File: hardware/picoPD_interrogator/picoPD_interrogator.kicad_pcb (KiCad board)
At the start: 4 copper layers, 81.9 x 17.2 mm, 94 parts, among them J4 Extra Pins, J5 Conn_01x04, J6 SM03B-SRSS-TB, J7 SM04B-SRSS-TB, Q1 rohm-RE1C002UN, Q2 rohm-RE1C002UN, Q3 rohm-RE1C002UN, Q4 rohm-RE1C002UN, Q5 rohm-RE1C002UN, Q6 rohm-RE1C002UN, SW1 SW_Push, SW2 SW_Push, U1 RP2350_60QFN, U10 W25Q128JVS, U2 ST-LM393QT, U7 LV2862XDDC, Y1 Crystal_GND24

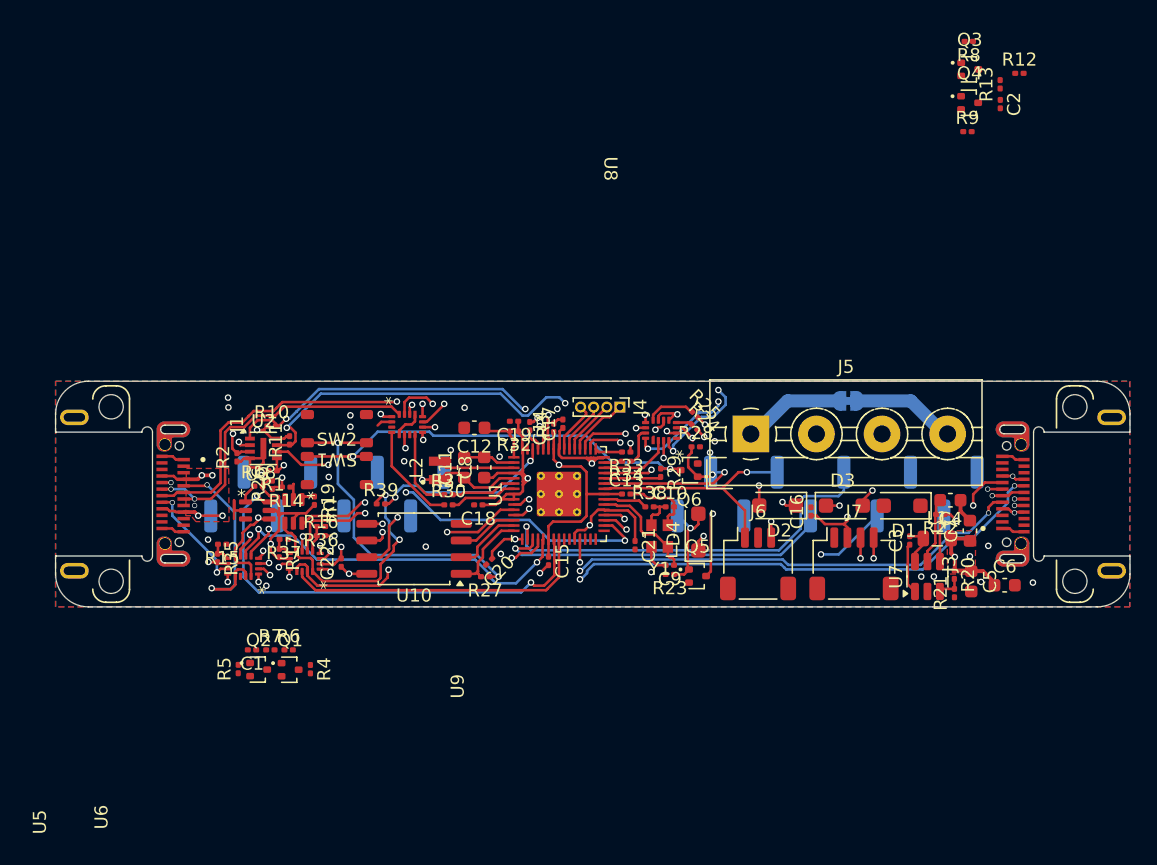
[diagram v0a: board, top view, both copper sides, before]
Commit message: Routed almost everything. Just need to finish VBUS tracks and check for any obvious issues.
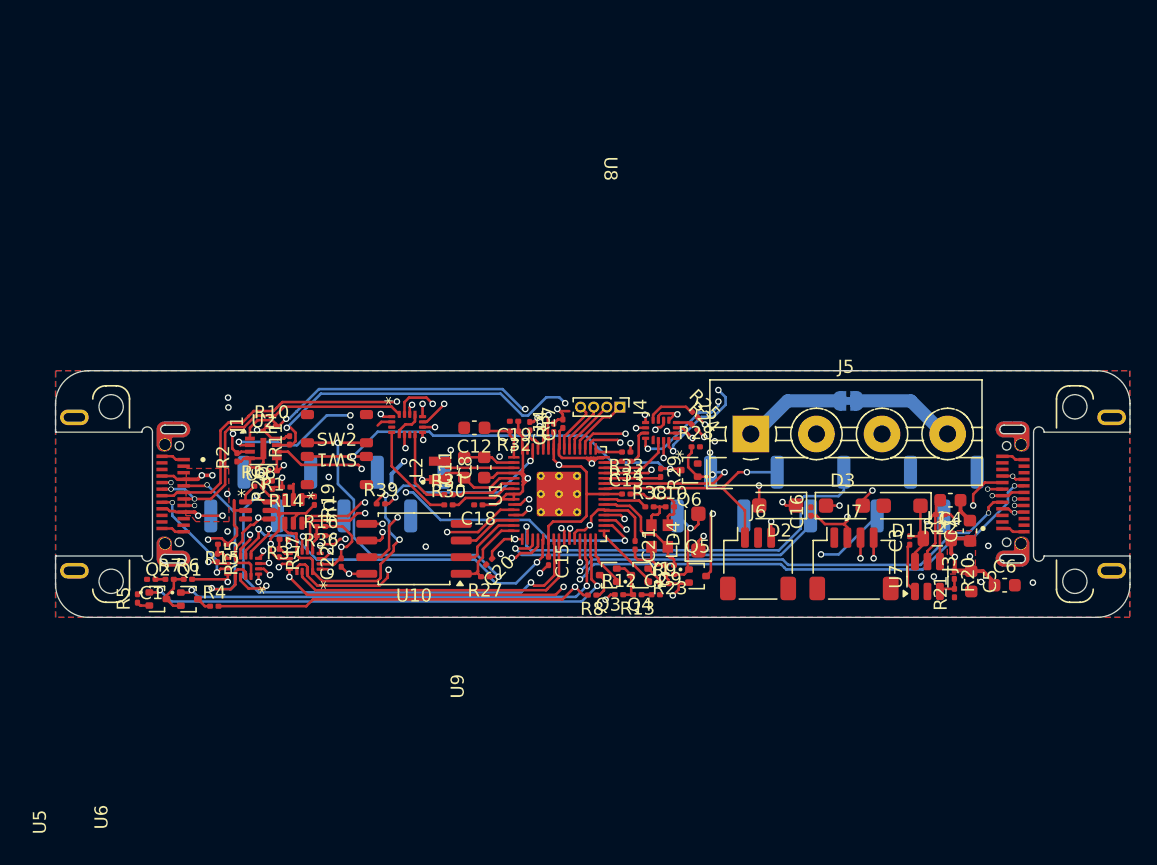
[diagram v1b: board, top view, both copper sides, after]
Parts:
- moved R8 51.0 mm to (158.4, 107.7)
- moved R12 50.1 mm to (160.4, 107.7)
- moved R13 47.7 mm to (161.8, 107.7), turned to 180 degrees
- moved Q3 47.4 mm to (159.6, 106.2), turned to 180 degrees
- moved C2 45.7 mm to (163.2, 107.7), turned to 0 degrees
- moved Q4 43.9 mm to (162.0, 106.2), turned to 180 degrees
- moved R9 41.5 mm to (163.9, 106.8)
- moved R5 9.38 mm to (123.7, 108.0)
- moved R6 9.38 mm to (127.6, 106.5)
- moved R7 9.38 mm to (126.2, 106.5)
- moved C1 9.38 mm to (124.8, 106.5)
- moved Q1 9.38 mm to (127.7, 108.0)
- moved Q2 9.38 mm to (125.3, 108.0)
- moved R4 8.76 mm to (129.6, 108.5), turned to 0 degrees
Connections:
- Q3 pad 2: /USB_PD/P0_TX -> /USB_PD/P1_TX
- Q4 pad 3: /USB_PD/P0_TX -> /USB_PD/P1_TX
- R12 pad 2: /USB_PD/P0_TX -> /USB_PD/P1_TX
- R13 pad 2: /USB_PD/P0_TX -> /USB_PD/P1_TX
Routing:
- net /P1_CC_RX: track 26.8 -> 66.5 mm, vias 2 -> 4
- net /P0_TX_L: track 0.00 -> 38.9 mm, vias 0 -> 2
- net /P0_CC_RX: track 24.3 -> 60.2 mm, vias 2 -> 4
- net /P0_TX_H: track 0.00 -> 35.2 mm, vias 0 -> 2
- net /P1_CC: track 35.4 -> 65.7 mm, vias 5 -> 9
- net /3V3: track 75.1 -> 104.1 mm, vias 16 -> 17
- net GND: track 38.1 -> 59.5 mm, vias 17 -> 18
- net /REG_VIN: track 7.53 -> 20.1 mm, vias 2 -> 3
- net /P0_CC: track 42.1 -> 54.5 mm, vias 6 -> 5
- net /RP2350A/1V1: track 24.6 -> 35.5 mm
- net /P1_TX_L: track 0.00 -> 5.27 mm
- net /P1_TX_H: track 0.00 -> 3.91 mm
- net /USB_PD/P0_TX: track 0.00 -> 3.80 mm
- net /USB_PD/P1_TX: track 0.00 -> 3.62 mm
- net /P0_ORIENT: track 22.7 -> 25.3 mm
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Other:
- board size 81.9 x 17.2 mm -> 81.9 x 18.8 mm

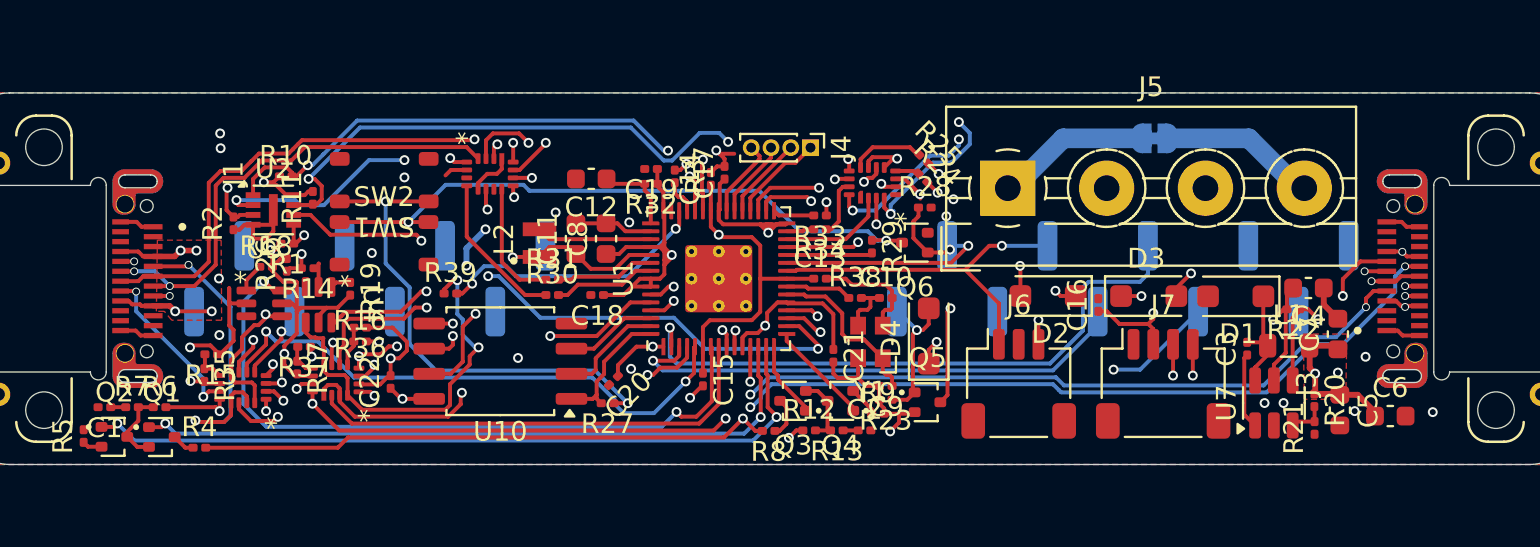
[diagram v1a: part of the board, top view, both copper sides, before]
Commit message: PCB: Resolve a bunch of clearance DRC errors.
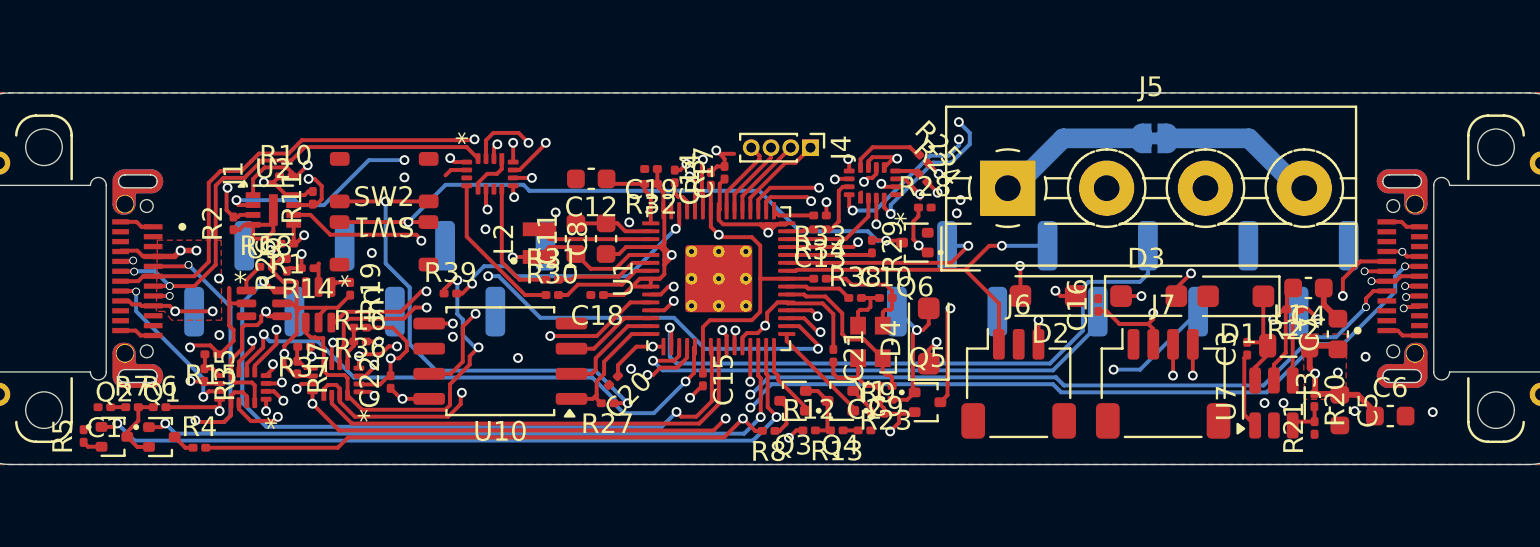
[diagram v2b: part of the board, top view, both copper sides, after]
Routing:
- net /P1_CC_RX: track 66.5 -> 42.8 mm, vias 4 -> 3
- net /P0_CC_RX: track 60.2 -> 40.4 mm, vias 4 -> 3
- net /P0_CC: track 54.5 -> 58.3 mm
- net /P0_VBUS: track 23.8 -> 26.3 mm
- net /P1_CC: track 65.7 -> 63.5 mm, vias 9 -> 8
- net /P0_VCONN: track 36.0 -> 37.2 mm
- net /P1_VBUS: track 20.6 -> 19.7 mm
- net /RP2_RESET: track 20.1 -> 20.9 mm
- net /USB_PD/P0_SBU2: vias 4 -> 3
- net /USB_PD/P0_SBU1: vias 3 -> 2

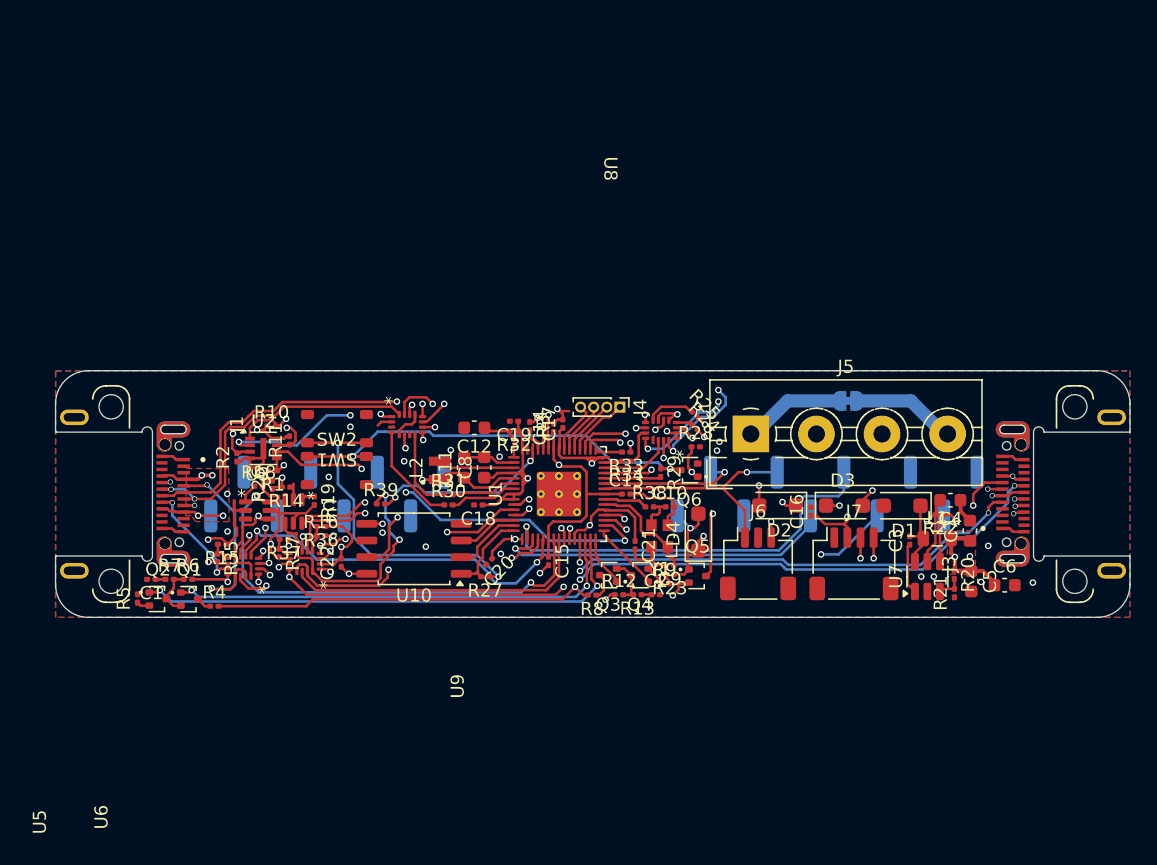
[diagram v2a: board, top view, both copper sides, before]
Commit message: Footprint/PCB: Modified JAE USB-C connector to have plated through-hole for the screw mount holes. Fixed missing SPI flash track.
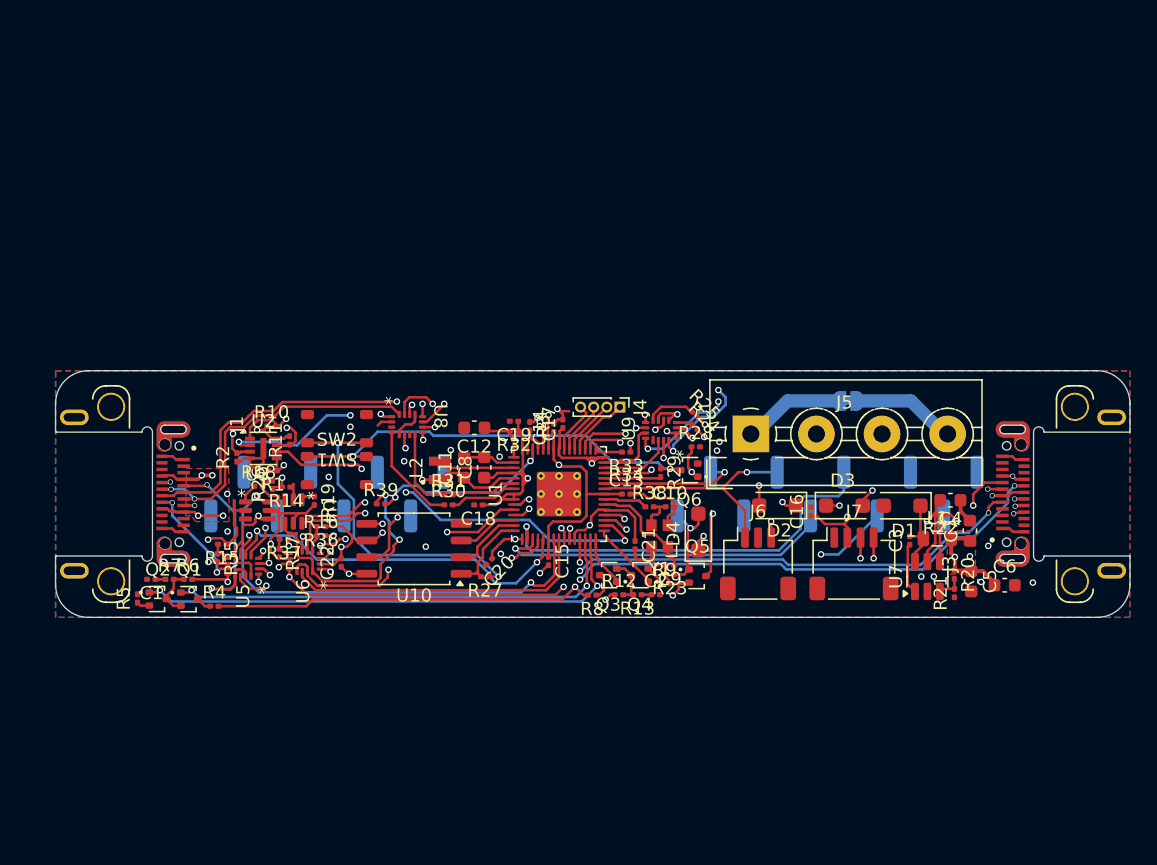
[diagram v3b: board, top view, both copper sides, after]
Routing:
- net /RP2350A/FLASH_CLK: track 12.2 -> 13.7 mm

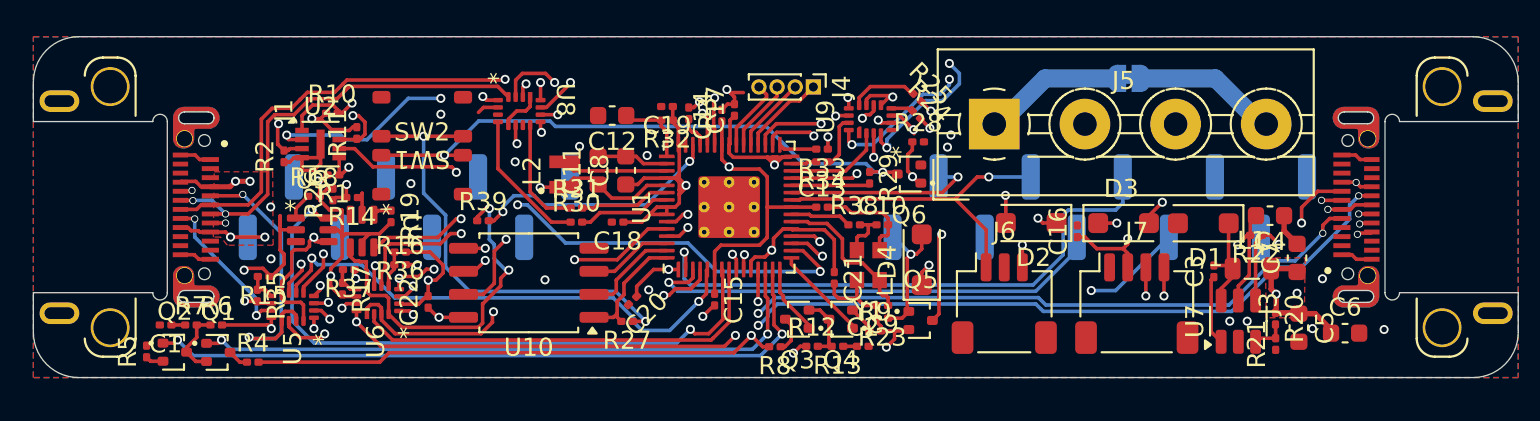
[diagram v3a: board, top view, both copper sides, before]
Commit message: PCB: Added silkscreen text and board revision. (Rev. C)
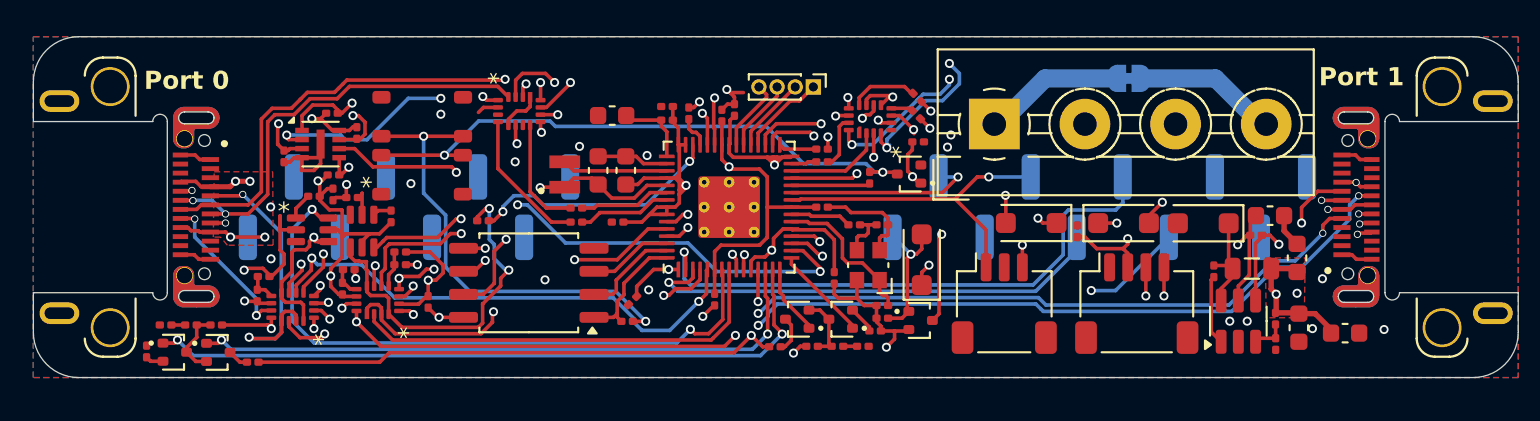
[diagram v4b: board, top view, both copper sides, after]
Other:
- board text added: "Port 0"
- board text added: "Port 1"
- board text added: "Rev. C"
- board text added: "Samuel Hedrick"
- board text added: "VBUS"
- board text added: "https://github.com/Samuelrmlink/picoPD_interrogator"
- board text added: "rmLINK Technologies"
